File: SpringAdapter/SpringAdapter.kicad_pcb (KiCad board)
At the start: 2 copper layers, 32 x 32.1 mm, 17 parts, among them J1 USB_C_Receptacle_USB2.0, J2 Conn_02x04_Odd_Even, SW1 SW_DIP_x01, U1 AP2112K-3.3

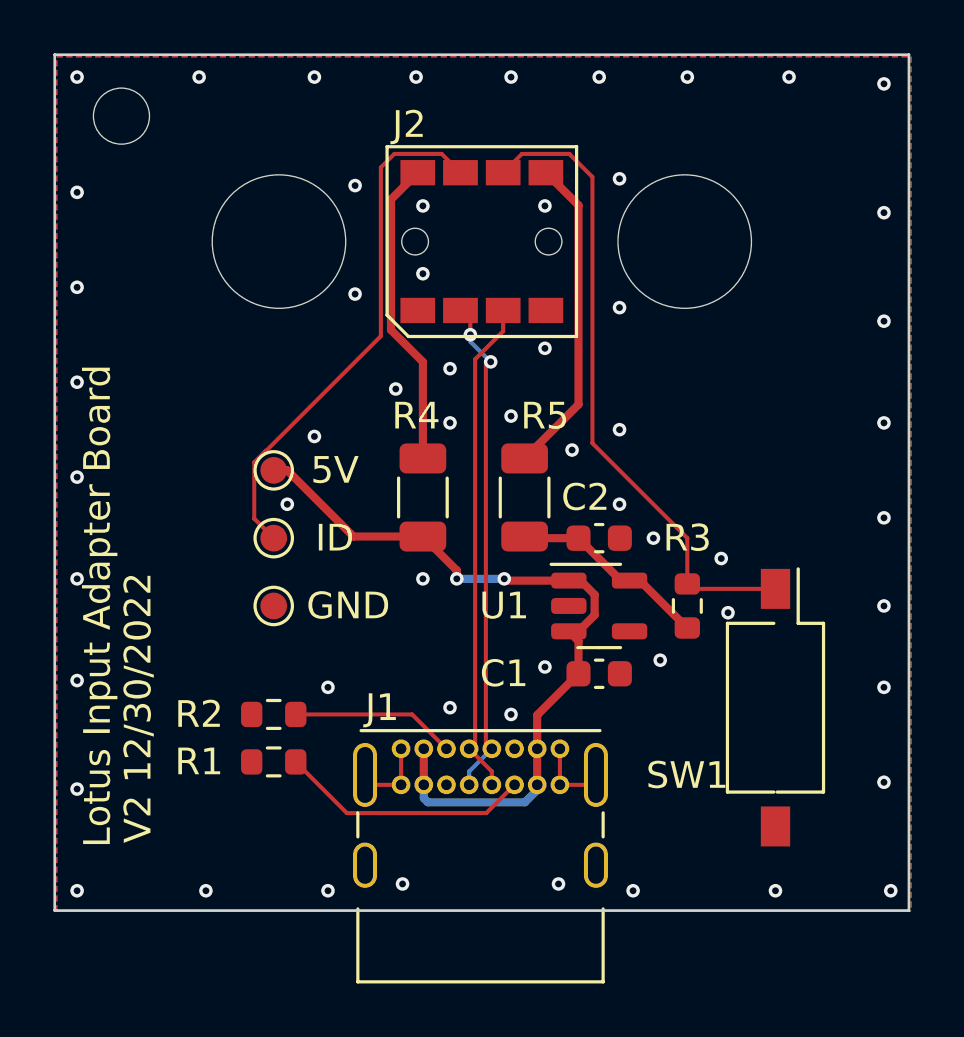
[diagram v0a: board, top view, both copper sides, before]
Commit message: Add second mounting hole
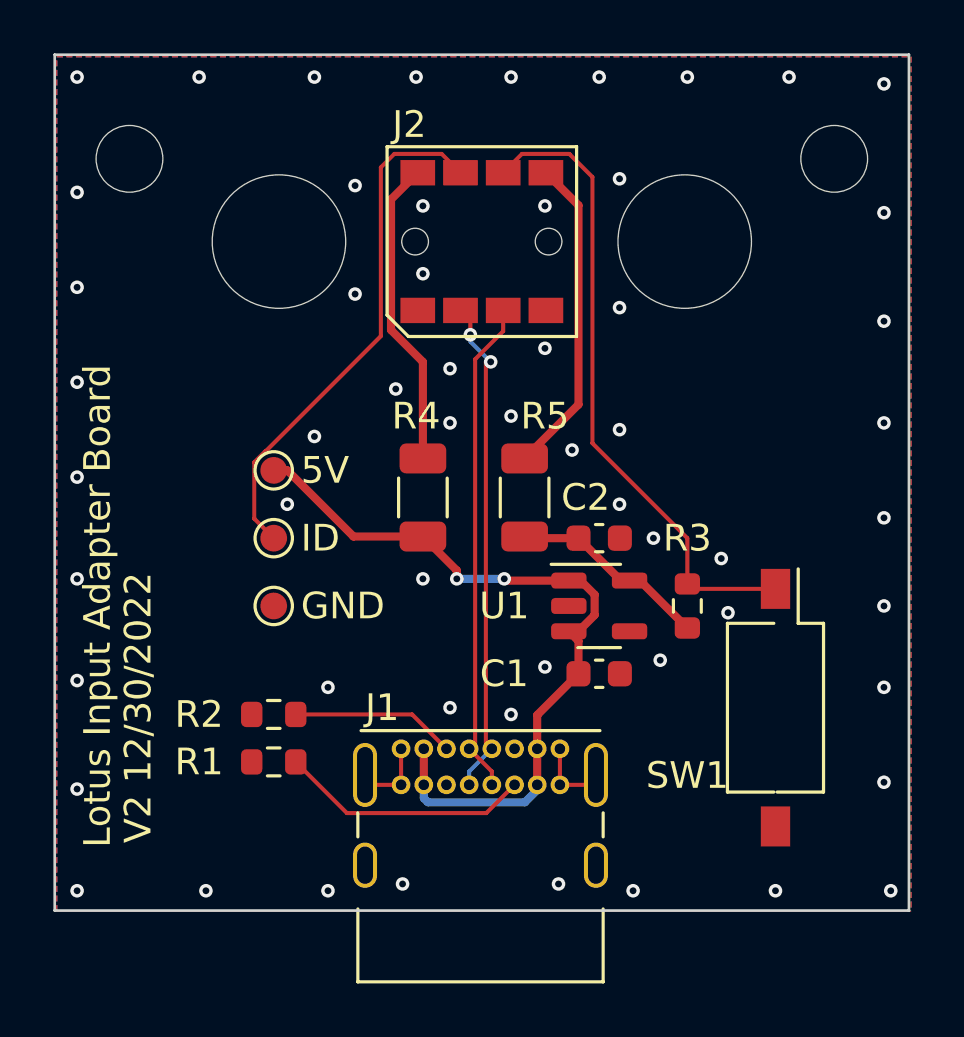
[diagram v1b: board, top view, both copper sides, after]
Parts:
- added e: MountingHole, MountingHole:MountingHole_2.5mm, F.Cu at (129.2, 103.9)
- Hb: renamed from H3; footprint MountingHole:MountingHole_2.1mm -> MountingHole:MountingHole_2.5mm
- moved Hb 1.63 mm to (102.8, 103.9)
- renumbered 5V to TP1, GND to TP2, ID to TP3
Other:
- board text added: "5V"
- board text added: "GND"
- board text added: "ID"
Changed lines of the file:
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@@
     )
   )
-  (footprint "MountingHole:MountingHole_2.1mm" (layer "F.Cu")
-    (at 102.5 102.3)
-    (descr "Mounting Hole 2.1mm, no annular")
-    (tags "mounting hole 2.1mm no annular")
+  (footprint "MountingHole:MountingHole_2.5mm" (layer "F.Cu")
+    (at 102.8 103.9)
+    (descr "Mounting Hole 2.5mm, no annular")
+    (tags "mounting hole 2.5mm no annular")
     (property "Sheetfile" "SpringAdapter.kicad_sch")
     (property "Sheetname" "")
     (attr exclude_from_pos_files)
-    (fp_text reference "H3" (at 0 -3.2) (layer "F.SilkS") hide
-      (effects (font (size 1 1) (thickness 0.15)))
-    )
-    (fp_text value "MountingHole" (at 0 3.2) (layer "F.Fab")
-      (effects (font (size 1 1) (thickness 0.15)))
-    )
-    (fp_text user "${REFERENCE}" (at 0 0) (layer "F.Fab")
-      (effects (font (size 1 1) (thickness 0.15)))
-    )
-    (fp_circle (center 0 0) (end 1.05 0) (layer "Cmts.User") (width 0.15) (fill none))
-    (fp_circle (center 0 0) (end 1.35 0) (layer "F.CrtYd") (width 0.05) (fill none))
-    (pad "" np_thru_hole circle (at 0 0) (size 2.1 2.1) (drill 2.1) (layers *.Cu *.Mask))
+    (fp_text reference "Hb" (at 0 -3.5) (layer "F.SilkS") hide
+      (effects (font (size 1 1) (thickness 0.15)))
+    )
+    (fp_text value "MountingHole" (at 0 3.5) (layer "F.Fab")
+      (effects (font (size 1 1) (thickness 0.15)))
+    )
+    (fp_text user "${REFERENCE}" (at 0 0) (layer "F.Fab")
+      (effects (font (size 1 1) (thickness 0.15)))
+    )
+    (fp_circle (center 0 0) (end 2.5 0) (layer "Cmts.User") (width 0.15) (fill none))
+    (fp_circle (center 0 0) (end 2.75 0) (layer "F.CrtYd") (width 0.05) (fill none))
+    (pad "" np_thru_hole circle (at 0 0) (size 2.5 2.5) (drill 2.5) (layers *.Cu *.Mask))
   )
   (footprint "Capacitor_SMD:C_0603_1608Metric" (layer "F.Cu")
@@
     (property "Sheetname" "")
     (attr exclude_from_pos_files)
-    (fp_text reference "5V" (at 2.286 0) (layer "F.SilkS")
+    (fp_text reference "TP1" (at 2.286 0) (layer "F.SilkS") hide
       (effects (font (size 1 1) (thickness 0.15)))
     )
@@
     )
   )
+  (footprint "MountingHole:MountingHole_2.5mm" (layer "F.Cu")
+    (at 129.2 103.9)
+    (descr "Mounting Hole 2.5mm, no annular")
+    (tags "mounting hole 2.5mm no annular")
+    (property "Sheetfile" "SpringAdapter.kicad_sch")
+    (property "Sheetname" "")
+    (attr exclude_from_pos_files)
+    (fp_text reference "e" (at 0 -3.5) (layer "F.SilkS") hide
+      (effects (font (size 1 1) (thickness 0.15)))
+    )
+    (fp_text value "MountingHole" (at 0 3.5) (layer "F.Fab")
+      (effects (font (size 1 1) (thickness 0.15)))
+    )
+    (fp_text user "${REFERENCE}" (at 0 0) (layer "F.Fab")
+      (effects (font (size 1 1) (thickness 0.15)))
+    )
+    (fp_circle (center 0 0) (end 2.5 0) (layer "Cmts.User") (width 0.15) (fill none))
+    (fp_circle (center 0 0) (end 2.75 0) (layer "F.CrtYd") (width 0.05) (fill none))
+    (pad "" np_thru_hole circle (at 0 0) (size 2.5 2.5) (drill 2.5) (layers *.Cu *.Mask))
+  )
   (footprint "TestPoint:TestPoint_Pad_D1.0mm" (layer "F.Cu")
     (at 108.204 120.65)
@@
     (property "Sheetname" "")
     (attr exclude_from_pos_files)
-    (fp_text reference "GND" (at 2.794 0) (layer "F.SilkS")
+    (fp_text reference "TP2" (at 2.794 0) (layer "F.SilkS") hide
       (effects (font (size 1 1) (thickness 0.15)))
     )
@@
     (property "Sheetname" "")
     (attr exclude_from_pos_files)
-    (fp_text reference "ID" (at 2.286 0) (layer "F.SilkS")
+    (fp_text reference "TP3" (at 2.286 0) (layer "F.SilkS") hide
       (effects (font (size 1 1) (thickness 0.15)))
     )
@@
   )
   (gr_rect (start 100 100) (end 132 132.06) (layer "Edge.Cuts") (width 0.1) (fill none))
+  (gr_text "GND" (at 109.22 120.65) (layer "F.SilkS")
+    (effects (font (size 1 1) (thickness 0.15)) (justify left))
+  )
   (gr_text "V2 12/30/2022" (at 103.124 124.46 90) (layer "F.SilkS")
     (effects (font (size 1 1) (thickness 0.15)))
@@
     (effects (font (size 1 1) (thickness 0.15)))
   )
+  (gr_text "ID" (at 109.22 118.11) (layer "F.SilkS")
+    (effects (font (size 1 1) (thickness 0.15)) (justify left))
+  )
+  (gr_text "5V" (at 109.22 115.57) (layer "F.SilkS")
+    (effects (font (size 1 1) (thickness 0.15)) (justify left))
+  )
   (segment (start 119.614184 121.6) (end 120.2258 120.988384) (width 0.3048) (layer "F.Cu") (net 1))

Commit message: correct spring position
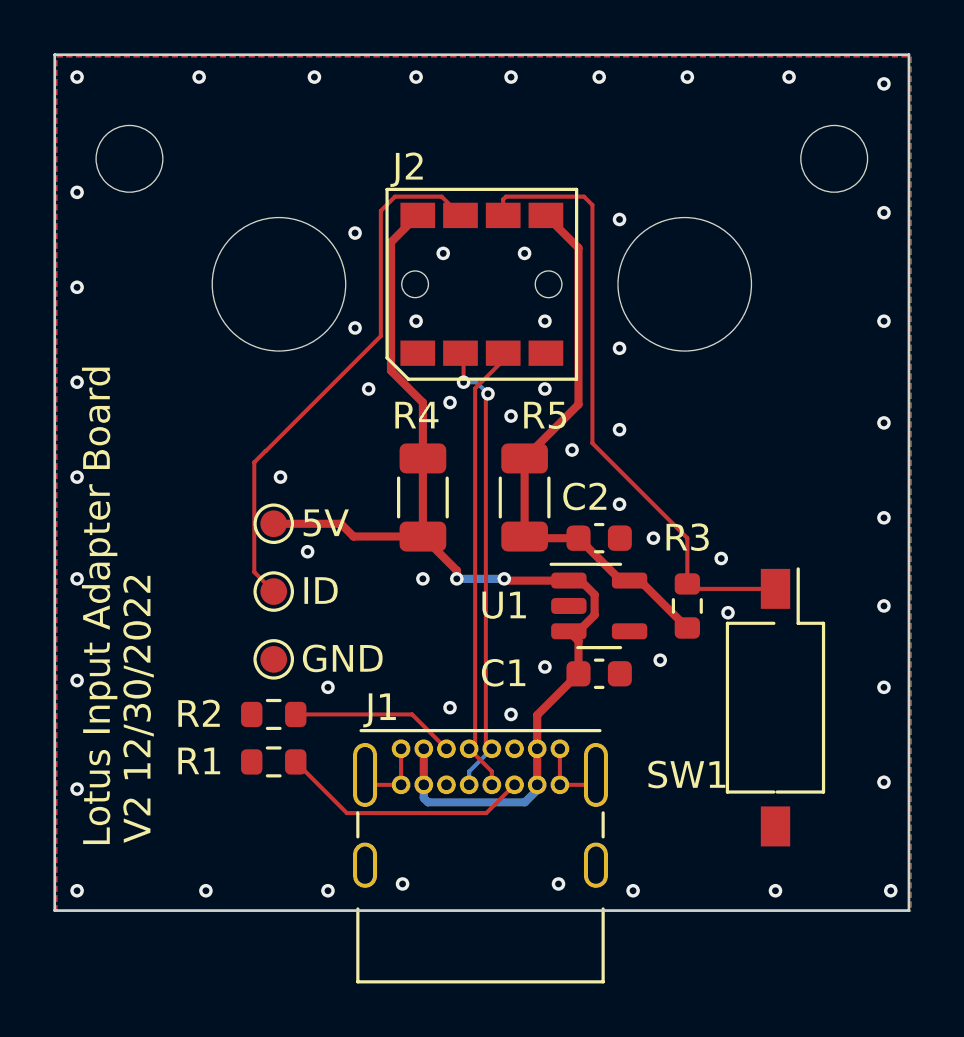
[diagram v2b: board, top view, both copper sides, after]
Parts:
- moved TP1 2.00 mm to (108.2, 117.6)
- moved TP2 2.00 mm to (108.2, 122.7)
- moved TP3 2.00 mm to (108.2, 120.1)
- moved H1 1.60 mm to (123.6, 108.6)
- moved H2 1.60 mm to (108.4, 108.6)
- moved J2 1.60 mm to (116.0, 108.6)
- renumbered Hb to H3, e to H4
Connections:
- J2 pad 2: Net-(J2-Pad2) -> +5V
- J2 pad 8: Net-(J2-Pad8) -> +3.3V
- R4 pad 2: Net-(J2-Pad2) -> +5V
- R5 pad 2: Net-(J2-Pad8) -> +3.3V
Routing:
- net +3.3V: track 7.52 -> 20.9 mm
- net +5V: track 29.2 -> 41.3 mm
- net Net-(J2-Pad8): track 12.0 -> 0.00 mm
- net Net-(J2-Pad2): track 11.6 -> 0.00 mm
- net /USB_D_N: track 18.9 -> 17.2 mm
- net /USB_D_P: track 18.7 -> 17.1 mm
- net /~{SLEEP}: track 24.1 -> 23.2 mm

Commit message: Update PCB rev
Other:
- board text added: "V3 02/14/2023"
- board text removed: "V2 12/30/2022"
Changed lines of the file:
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@@
     (effects (font (size 1 1) (thickness 0.15)) (justify left))
   )
-  (gr_text "V2 12/30/2022" (at 103.124 124.46 90) (layer "F.SilkS")
+  (gr_text "V3 02/14/2023" (at 103.124 124.46 90) (layer "F.SilkS")
     (effects (font (size 1 1) (thickness 0.15)))
   )

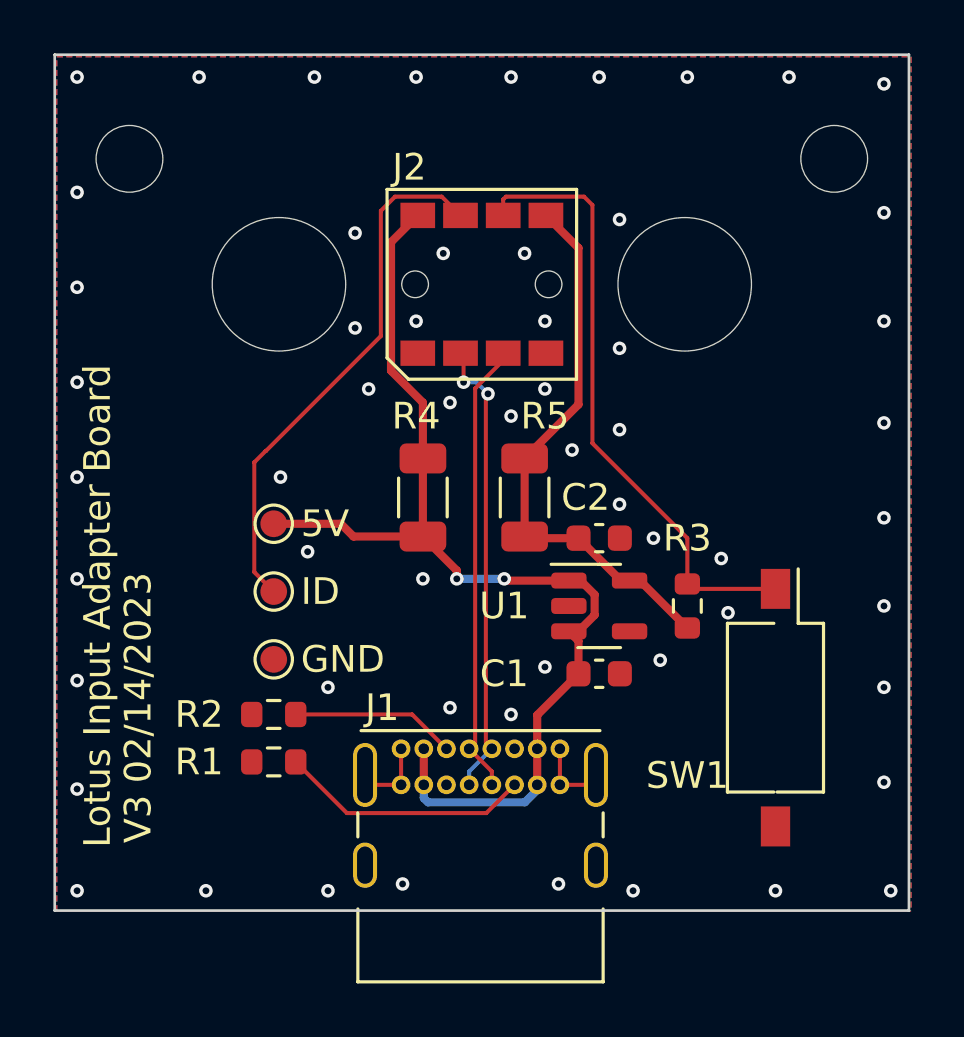
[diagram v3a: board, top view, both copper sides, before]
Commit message: Switch to pogo pins
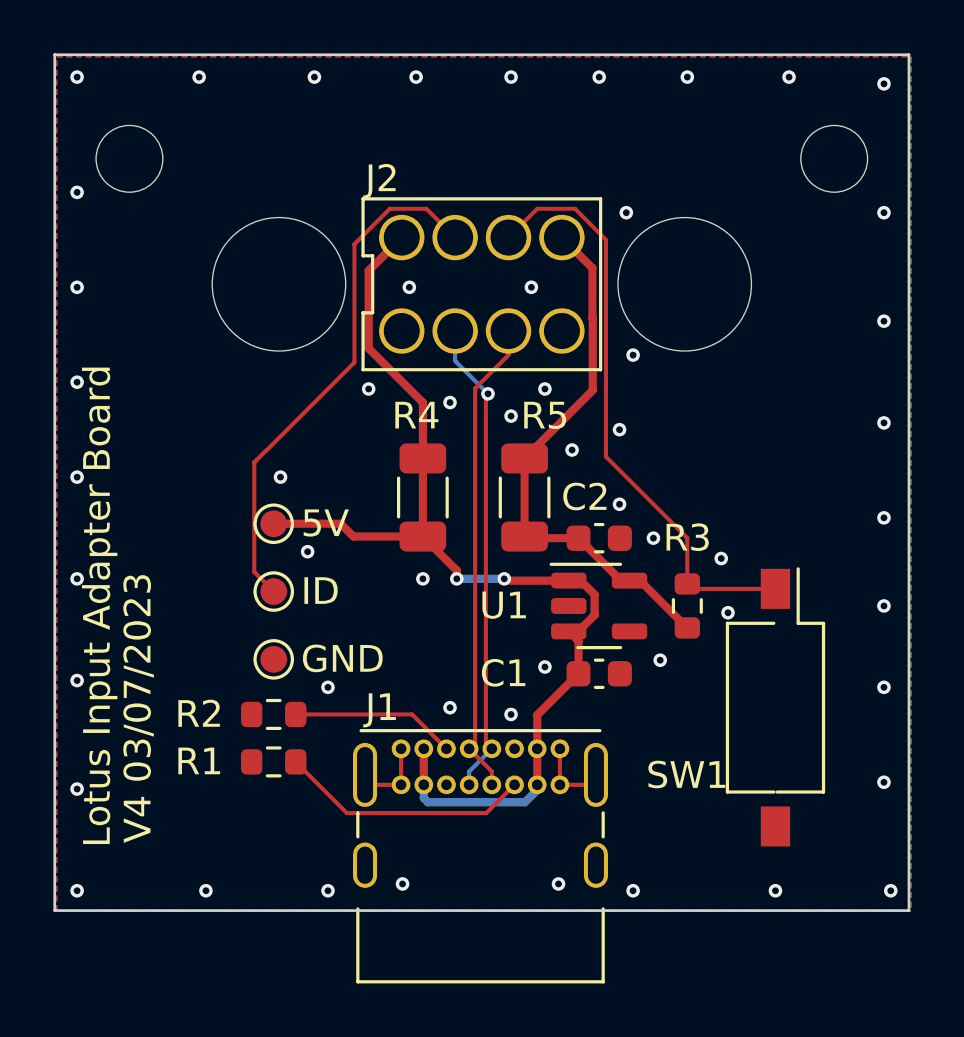
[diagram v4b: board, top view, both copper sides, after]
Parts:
- J2: footprint SpringAdapter:ABTBA018_2x4_P1.6mm -> SpringAdapter:BP33242_2x4_P2.0mm
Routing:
- net /~{SLEEP}: track 23.2 -> 22.1 mm
- net /USB_D_P: track 17.1 -> 18.0 mm
- net /USB_D_N: track 17.2 -> 18.0 mm, vias 2 -> 1
- net +3.3V: track 20.9 -> 20.2 mm
- net GND: vias 57 -> 53
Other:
- board text added: "V4 03/07/2023"
- board text removed: "V3 02/14/2023"
